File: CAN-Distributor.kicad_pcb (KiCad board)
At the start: 2 copper layers, 66 x 115 mm, 18 parts, among them J1 RJ45, J10 RJ45, J2 RJ45, J3 RJ45, J4 RJ45, J5 RJ45, J6 RJ45, J7 RJ45, J8 RJ45, J9 RJ45

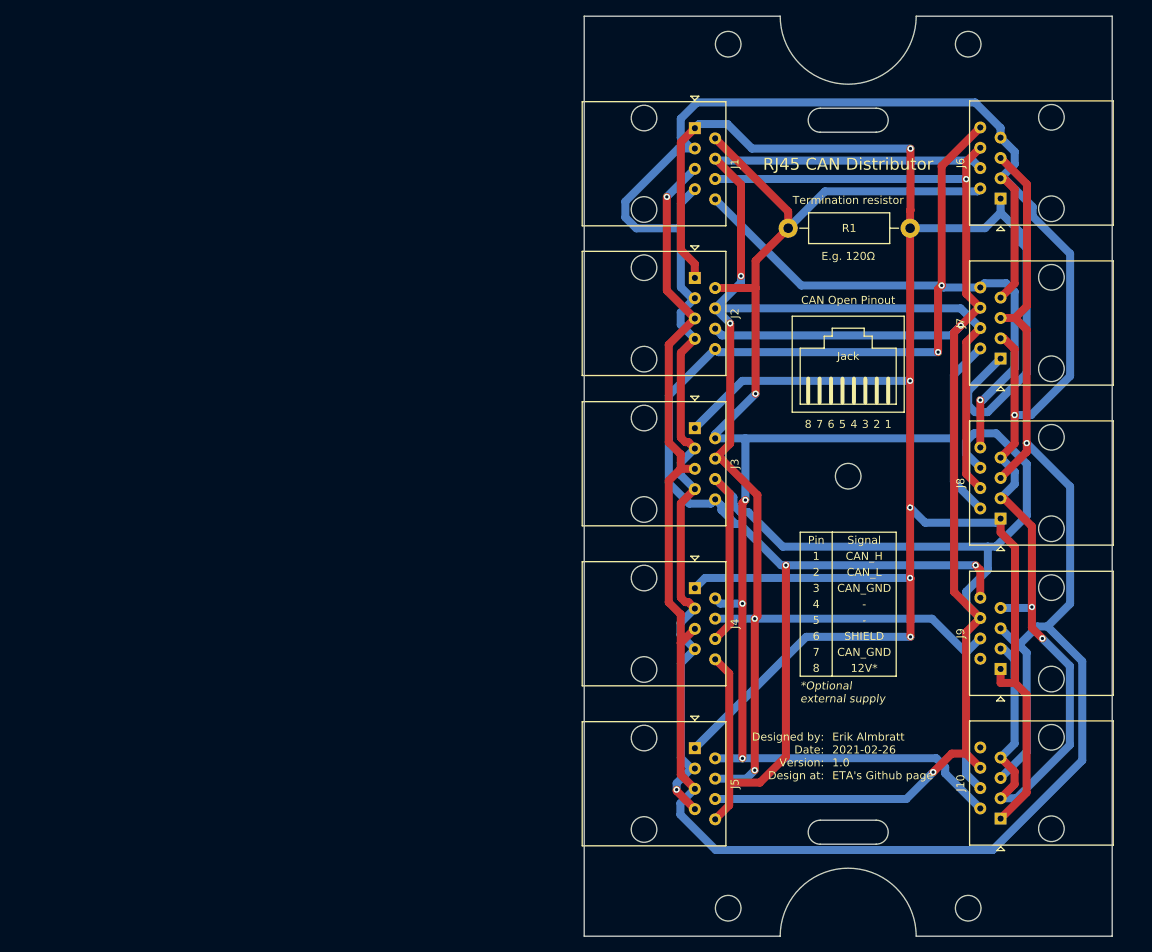
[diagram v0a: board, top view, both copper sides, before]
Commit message: Perform layout. Add CAN testpoints.
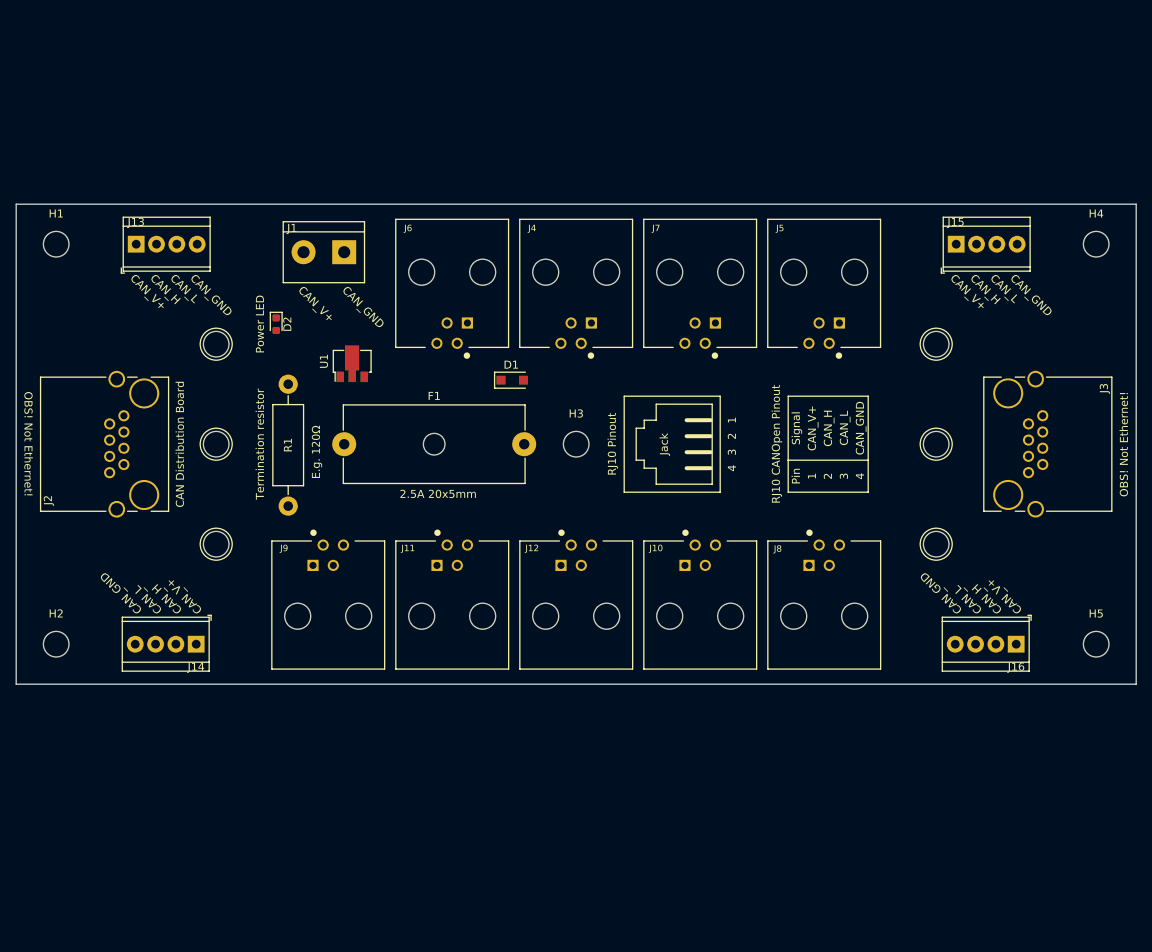
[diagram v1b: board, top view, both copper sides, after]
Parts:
- removed REF**: MountingHole_3.2mm_M3, MountingHole:MountingHole_3.2mm_M3
- added D1: D_Schottky, Diode_SMD:D_SOD-123F, F.Cu at (113.3, 87.2)
- added D2: PWR_LED, Diode_SMD:D_0603_1608Metric, F.Cu at (83.8, 80.2)
- added F1: 2.5A, Fuse:Fuseholder_Cylinder-5x20mm_Schurter_0031_8201_Horizontal_Open, F.Cu at (92.3, 95.2)
- added H5: MountingHole_3.2mm_M3_DIN965, MountingHole:MountingHole_3.2mm_M3_DIN965, F.Cu at (186.3, 120.2)
- added J11: RJ10, CAN-Distributor:TE_5520257-2, F.Cu at (105.8, 116.7)
- added J12: RJ10, CAN-Distributor:TE_5520257-2, F.Cu at (121.3, 116.7)
- added J13: 4p Terminal Block, TerminalBlock_TE-Connectivity:TerminalBlock_TE_282834-4_1x04_P2.54mm_Horizontal, F.Cu at (66.3, 70.2)
- added J14: 4p Terminal Block, TerminalBlock_TE-Connectivity:TerminalBlock_TE_282834-4_1x04_P2.54mm_Horizontal, F.Cu at (73.8, 120.2)
- added J15: 4p Terminal Block, TerminalBlock_TE-Connectivity:TerminalBlock_TE_282834-4_1x04_P2.54mm_Horizontal, F.Cu at (168.8, 70.2)
- added J16: 4p Terminal Block, TerminalBlock_TE-Connectivity:TerminalBlock_TE_282834-4_1x04_P2.54mm_Horizontal, F.Cu at (176.3, 120.2)
- added M1: DINRailAdapter_3xM3_PhoenixContact_1201578, MountingEquipment:DINRailAdapter_3xM3_PhoenixContact_1201578, F.Cu at (76.3, 95.2)
- added M2: DINRailAdapter_3xM3_PhoenixContact_1201578, MountingEquipment:DINRailAdapter_3xM3_PhoenixContact_1201578, F.Cu at (166.3, 95.2)
- added U1: CL25N8-G, Package_TO_SOT_SMD:SOT-89-3, F.Cu at (93.3, 85.1)
- G1: value CAN_Open_Pinout_Table_Silkscreen -> RJ10_CAN_Open_Pinout_Table_Silkscreen; footprint RJ45-CAN-Distributor:CAN_Open_Pinout_Table_Silkscreen -> CAN-Distributor:RJ10_CAN_Open_Pinout_Table_Silkscreen
- G2: value CAN_Open_Pinout_Silkscreen -> RJ10_Pinout_Silkscreen; footprint RJ45-CAN-Distributor:CAN_Open_Pinout_Silkscreen -> CAN-Distributor:RJ10_Pinout_Silkscreen
- H1, H2, H3, H4: value MountingHole_3.2mm_M3 -> MountingHole_3.2mm_M3_DIN965; footprint MountingHole:MountingHole_3.2mm_M3 -> MountingHole:MountingHole_3.2mm_M3_DIN965
- J1: value RJ45 -> 2p Terminal Block; footprint Connector_RJ:RJ45_Amphenol_54602-x08_Horizontal -> TerminalBlock:TerminalBlock_bornier-2_P5.08mm
- J10, J4, J5, J6, J7, J8, J9: value RJ45 -> RJ10; footprint Connector_RJ:RJ45_Amphenol_54602-x08_Horizontal -> CAN-Distributor:TE_5520257-2
- J2, J3: value RJ45 -> RJ45_Shielded; footprint Connector_RJ:RJ45_Amphenol_54602-x08_Horizontal -> CAN-Distributor:RJHSE5480
- moved H2 90.2 mm to (56.4, 120.2)
- moved H1 87.6 mm to (56.4, 70.2)
- moved H4 84.5 mm to (186.3, 70.2)
- moved J9 84.3 mm to (90.3, 116.7), turned to 0 degrees
- moved J2 71.9 mm to (67.3, 95.2), turned to 90 degrees
- moved H3 70.0 mm to (121.3, 95.2)
- moved J6 69.2 mm to (105.8, 73.7), turned to 180 degrees
- moved R1 65.5 mm to (85.3, 87.7), turned to 270 degrees
- moved J5 61.7 mm to (152.3, 73.7), turned to 180 degrees
- moved J1 46.5 mm to (92.3, 71.2), turned to 180 degrees
- moved J10 45.3 mm to (136.8, 116.7), turned to 0 degrees
- moved J4 42.2 mm to (121.3, 73.7), turned to 180 degrees
- moved J3 39.2 mm to (175.3, 95.2)
- moved J7 39.1 mm to (136.8, 73.7), turned to 180 degrees
- moved J8 25.2 mm to (152.3, 116.7), turned to 0 degrees
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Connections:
- J1 pad 1: CAN_H -> CAN_GND
- J1 pad 2: CAN_L -> Net-(F1-Pad1)
- J10 pad 1: CAN_H -> CAN_V+
- J10 pad 2: CAN_L -> CAN_H
- J10 pad 3: CAN_GND -> CAN_L
- J10 pad 4: Reserved1 -> CAN_GND
- J2 pad 4: Reserved1 -> Net-(J2-Pad4)
- J2 pad 5: Reserved2 -> Net-(J2-Pad5)
- J2 pad 6: SHIELD -> CAN_SHLD
- J2 pad 8: CAN_V+ -> Net-(J2-Pad8)
- J3 pad 4: Reserved1 -> Net-(J3-Pad4)
- J3 pad 5: Reserved2 -> Net-(J3-Pad5)
- J3 pad 6: SHIELD -> CAN_SHLD
- J3 pad 8: CAN_V+ -> Net-(J3-Pad8)
- J4 pad 1: CAN_H -> CAN_V+
- J4 pad 2: CAN_L -> CAN_H
- J4 pad 3: CAN_GND -> CAN_L
- J4 pad 4: Reserved1 -> CAN_GND
- J5 pad 1: CAN_H -> CAN_V+
- J5 pad 2: CAN_L -> CAN_H
- J5 pad 3: CAN_GND -> CAN_L
- J5 pad 4: Reserved1 -> CAN_GND
- J6 pad 1: CAN_H -> CAN_V+
- J6 pad 2: CAN_L -> CAN_H
- J6 pad 3: CAN_GND -> CAN_L
- J6 pad 4: Reserved1 -> CAN_GND
- J7 pad 1: CAN_H -> CAN_V+
- J7 pad 2: CAN_L -> CAN_H
- J7 pad 3: CAN_GND -> CAN_L
- J7 pad 4: Reserved1 -> CAN_GND
- J8 pad 1: CAN_H -> CAN_V+
- J8 pad 2: CAN_L -> CAN_H
- J8 pad 3: CAN_GND -> CAN_L
- J8 pad 4: Reserved1 -> CAN_GND
- J9 pad 1: CAN_H -> CAN_V+
- J9 pad 2: CAN_L -> CAN_H
- J9 pad 3: CAN_GND -> CAN_L
- J9 pad 4: Reserved1 -> CAN_GND
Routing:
- net CAN_GND: track 314.7 -> 0.00 mm, vias 4 -> 0
- net CAN_H: track 307.7 -> 0.00 mm, vias 5 -> 0
- net SHIELD: track 276.9 -> 0.00 mm, vias 3 -> 0
- net Reserved2: track 266.0 -> 0.00 mm, vias 2 -> 0
- net CAN_V+: track 243.0 -> 0.00 mm, vias 5 -> 0
- net Reserved1: track 231.4 -> 0.00 mm, vias 4 -> 0
- net CAN_L: track 208.8 -> 0.00 mm, vias 4 -> 0
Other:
- board size 66 x 115 mm -> 140 x 60 mm
- board text added: "2.5A 20x5mm"
- board text added: "CAN Distribution Board"
- board text added: "CAN_GND"
- board text added: "CAN_H"
- board text added: "CAN_L"
- board text added: "CAN_V+"
- board text added: "El Psy Congroo"
- board text added: "Erik Almbratt 2021-04-03 2.0 ETA's Github page"
- board text added: "OBS! Not Ethernet!"
- board text added: "Power LED"
- board text removed: "*Optional external supply"
- board text removed: "Erik Almbratt 2021-02-26 1.0 ETA's Github page"
- board text removed: "Laird RJ45-FT Cable feedthru"
- board text removed: "Maszczyk Z-74T (KMz 74) enclosure outline"
- board text removed: "RJ45 CAN Distributor"

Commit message: Autoroute board.
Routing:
- net CAN_GND: track 0.00 -> 346.0 mm, vias 0 -> 3
- net CAN_L: track 0.00 -> 343.6 mm, vias 0 -> 3
- net CAN_H: track 0.00 -> 314.4 mm, vias 0 -> 2
- net CAN_V+: track 0.00 -> 293.1 mm, vias 0 -> 1
- net CAN_SHLD: track 0.00 -> 157.4 mm
- net Net-(F1-Pad1): track 0.00 -> 26.1 mm
- net Net-(D2-Pad2): track 0.00 -> 12.1 mm
- net Net-(D1-Pad2): track 0.00 -> 8.04 mm
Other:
- net class Default: clearance 0.2 -> 0.15; trace_width 0.25 -> 1; via_dia 0.8 -> 0.6; via_drill 0.4 -> 0.3
- net class Power added: clearance 0.15, trace_width 1, via_dia 0.6, via_drill 0.3
- rule trace_clearance: 0.2 -> 0.15
- rule trace_min: 0.2 -> 0.127
- rule via_min_size: 0.4 -> 0.6

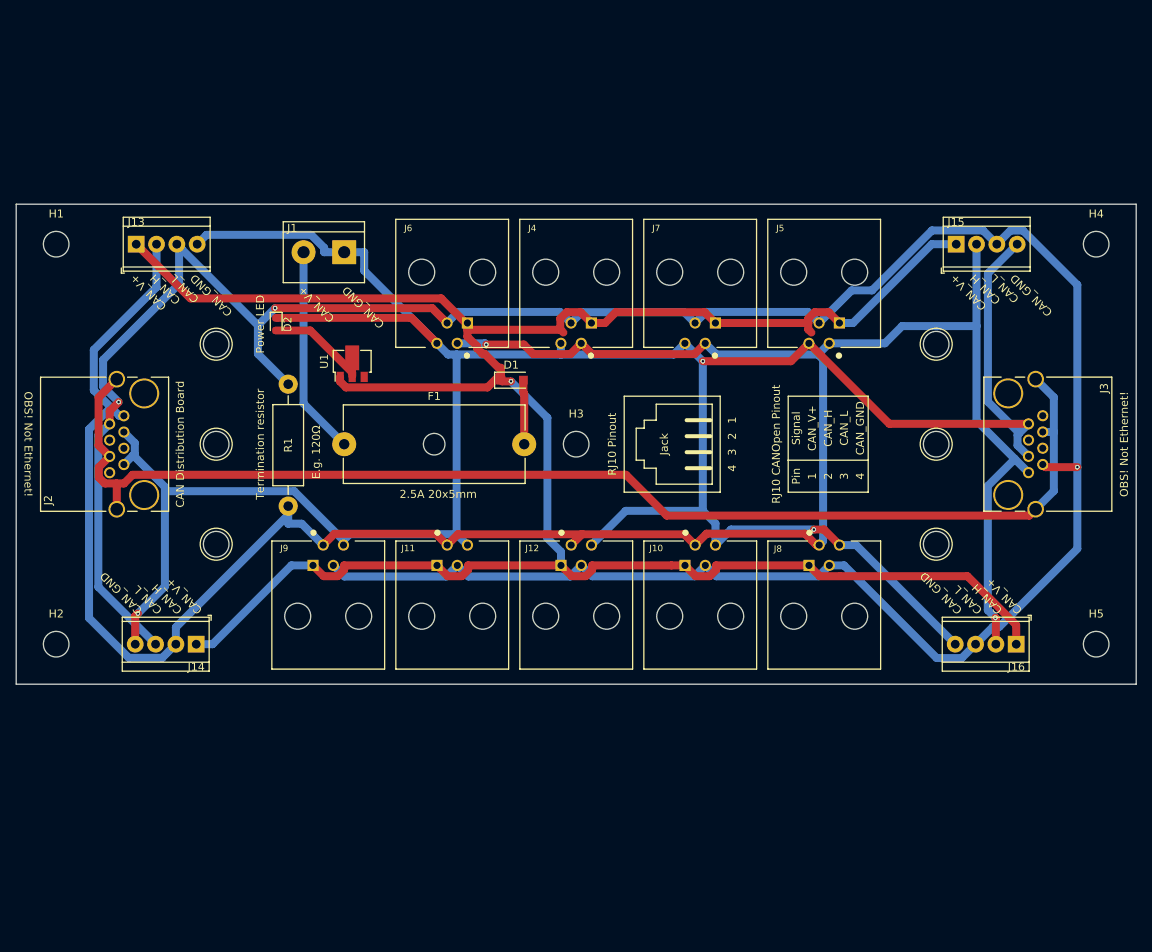
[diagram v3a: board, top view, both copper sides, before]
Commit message: Add a tenth RJ10 connector.
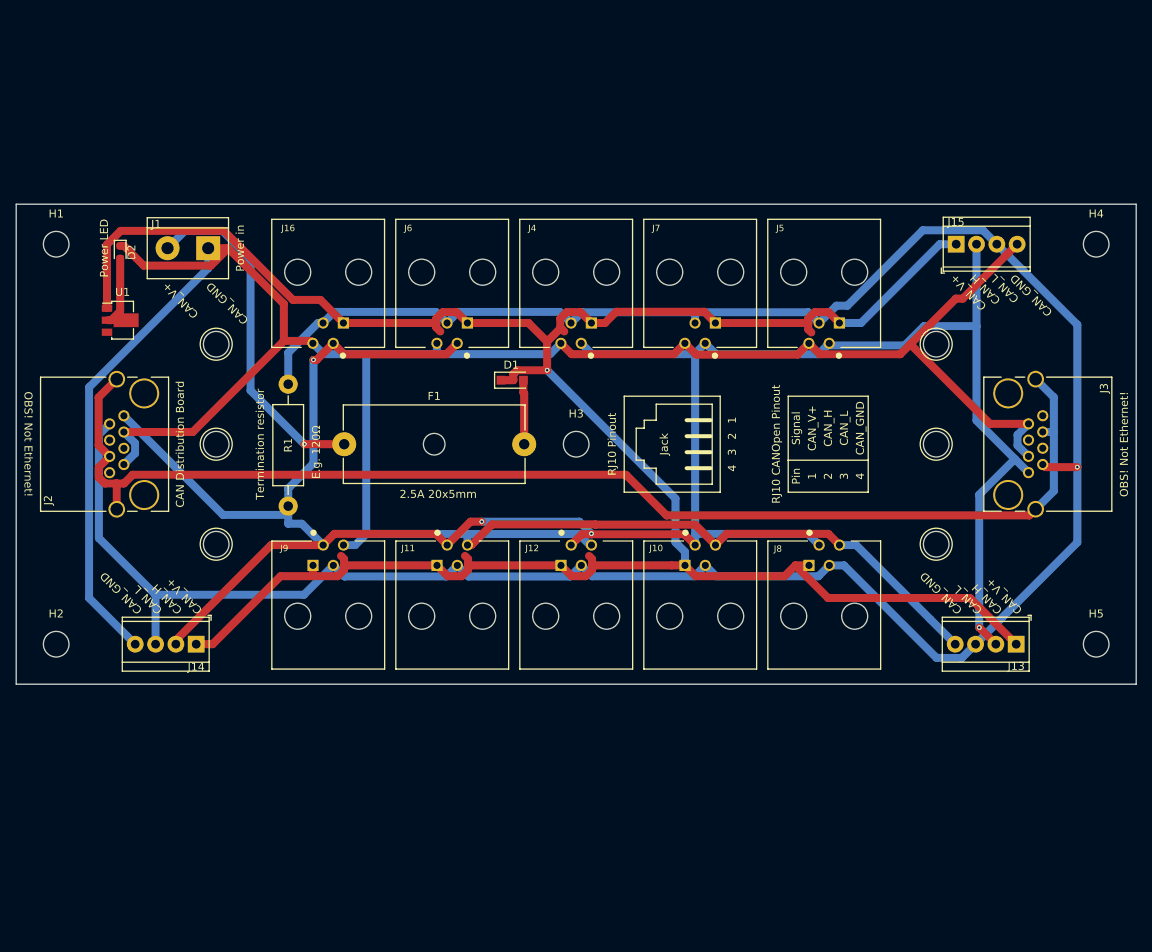
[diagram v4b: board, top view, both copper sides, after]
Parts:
- J16: value 4p Terminal Block -> RJ10; footprint TerminalBlock_TE-Connectivity:TerminalBlock_TE_282834-4_1x04_P2.54mm_Horizontal -> CAN-Distributor:TE_5520257-2
- moved J13 120.8 mm to (176.3, 120.2), turned to 180 degrees
- moved J16 97.8 mm to (90.3, 73.7)
- moved U1 29.5 mm to (64.3, 79.7), turned to 0 degrees
- moved D2 21.5 mm to (64.3, 71.2)
- moved J1 17.0 mm to (75.3, 70.7)
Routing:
- net CAN_L: track 343.6 -> 313.3 mm, vias 3 -> 1
- net CAN_GND: track 346.0 -> 372.7 mm, vias 3 -> 0
- net Net-(F1-Pad1): track 26.1 -> 43.6 mm, vias 0 -> 1
- net CAN_H: track 314.4 -> 300.0 mm, vias 2 -> 4
- net CAN_V+: track 293.1 -> 298.7 mm
- net Net-(D2-Pad2): track 12.1 -> 8.63 mm
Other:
- board text added: "Power in"

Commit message: Add protection TVS and GDT. Rename TP file.
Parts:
- added D3: TVS, Package_TO_SOT_SMD:SOT-23, F.Cu at (175.8, 108.7)
- added GD1: GDT, CAN-Distributor:Bourns_Inc.-2036-07-SM-RPLF-MFG, F.Cu at (183.9, 109.9)
- moved J8 0.07 mm to (152.3, 116.8)
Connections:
- J2 pad 6: CAN_SHLD -> CAN_GND
- J2 pad SH: CAN_SHLD -> CAN_GND
- J3 pad 6: CAN_SHLD -> CAN_GND
- J3 pad SH: CAN_SHLD -> CAN_GND
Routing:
- net CAN_SHLD: track 157.4 -> 0.00 mm
- net CAN_GND: track 372.7 -> 406.8 mm, vias 0 -> 2
- net CAN_H: track 300.0 -> 331.2 mm, vias 4 -> 1
- net Net-(F1-Pad1): track 43.6 -> 34.1 mm, vias 1 -> 0
- net CAN_L: track 313.3 -> 322.8 mm, vias 1 -> 2
- net CAN_V+: track 298.7 -> 290.0 mm, vias 1 -> 4
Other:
- board text added: "Erik Almbratt 2021-04-04 2.1 ETA's Github page"
- board text removed: "Erik Almbratt 2021-04-03 2.0 ETA's Github page"

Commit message: Add additional GND input
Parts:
- J1: value 2p Terminal Block -> 3p Terminal Block; footprint TerminalBlock:TerminalBlock_bornier-2_P5.08mm -> TerminalBlock:TerminalBlock_bornier-3_P5.08mm
- moved D2 10.8 mm to (58.1, 80.0)
- moved U1 1.01 mm to (64.2, 80.7), turned to 180 degrees
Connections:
- J1 pad 2: Net-(F1-Pad1) -> CAN_GND
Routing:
- net CAN_V+: track 290.0 -> 280.7 mm
- net CAN_GND: track 406.8 -> 415.6 mm, vias 2 -> 3
- net Net-(F1-Pad1): track 34.1 -> 39.1 mm
